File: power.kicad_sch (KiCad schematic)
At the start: 8 parts, among them J3 Screw_Terminal_01x02, J4 Screw_Terminal_01x02, U8 AZ1117CH-5.0TRG1, U9 LD29150DT33R

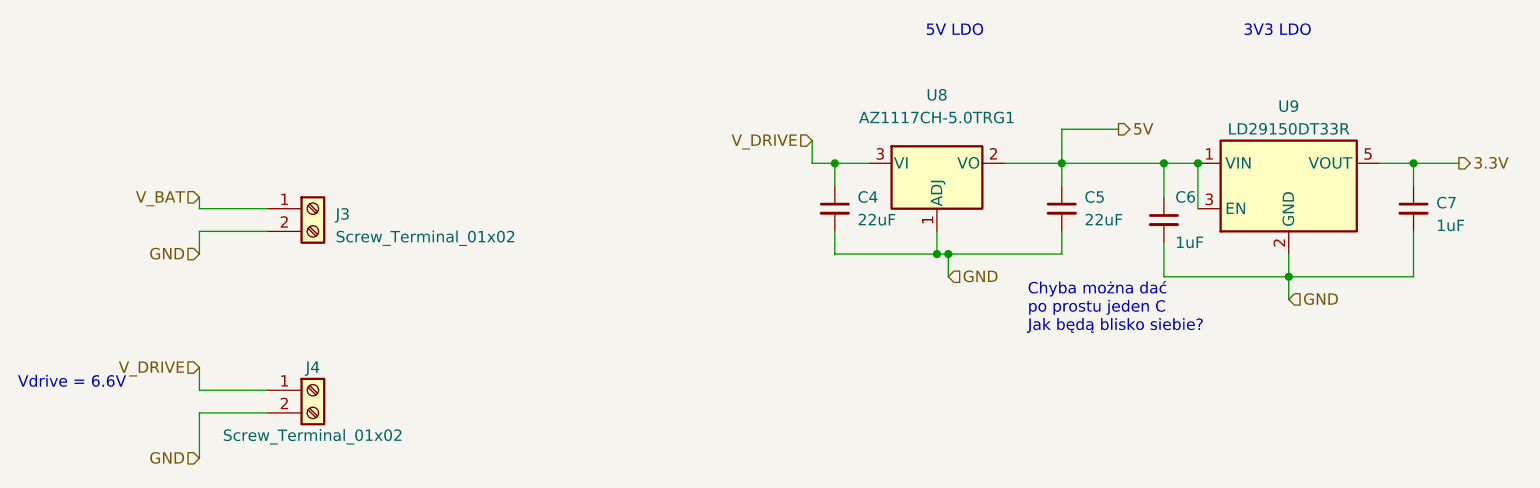
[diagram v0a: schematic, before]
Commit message: Bord v1.2, added flash memory, changed pinout od servomotor connectors and removed potentiometer signal from servomotors plus one ADC
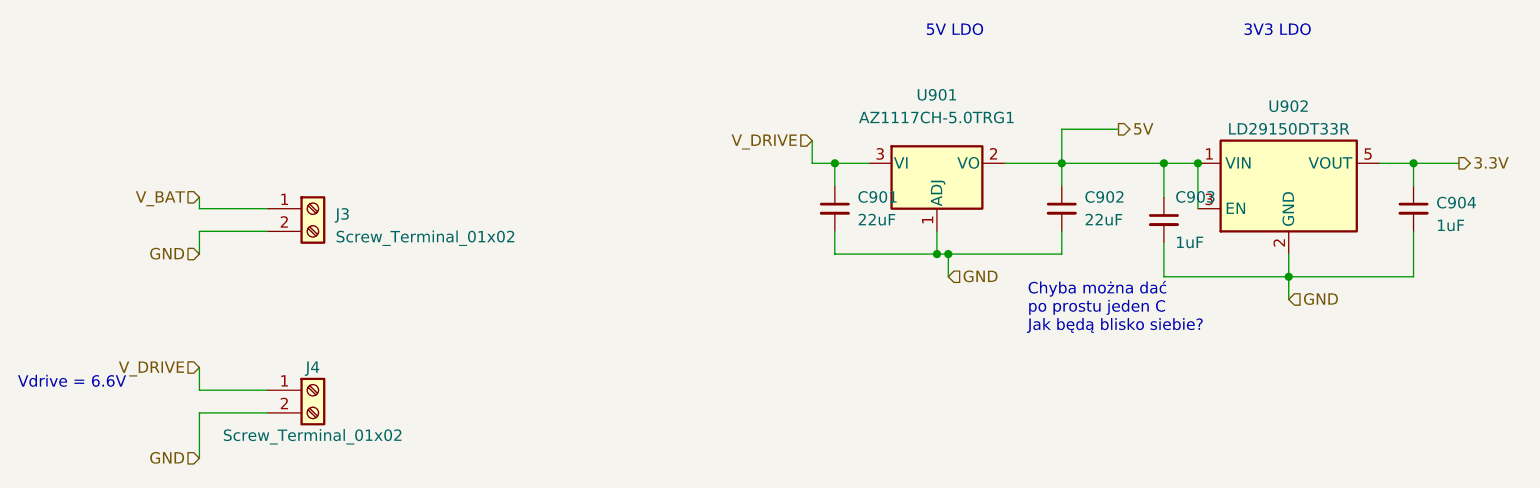
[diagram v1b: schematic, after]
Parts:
- renumbered C4 to C901, C5 to C902, C6 to C903, C7 to C904, U8 to U901, U9 to U902
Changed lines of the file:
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@@
   (symbol (lib_id "Device:C_Small") (at 156.21 63.5 0) (unit 1)
     (in_bom yes) (on_board yes) (dnp no)
-    (property "Reference" "C6" (at 157.48 60.96 0)
+    (property "Reference" "C903" (at 157.48 60.96 0)
       (effects (font (size 1.27 1.27)) (justify left))
     )
@@
       (project "Hexapod_Hardware"
         (path "/04005f68-61ba-4735-aba3-9cac296c0cce/2b79a7de-52ea-4f31-b6a5-c4c613c567f9"
+          (reference "C903") (unit 1)
+        )
+      )
+      (project "test_ADC_and_CurrentSensors"
+        (path "/11442fd4-c5b6-4318-b48c-3e08ddc782a8/1783009b-3fd4-4eb2-9eed-12da5fa53b67"
           (reference "C6") (unit 1)
         )
       )
-      (project "test_ADC_and_CurrentSensors"
-        (path "/11442fd4-c5b6-4318-b48c-3e08ddc782a8/1783009b-3fd4-4eb2-9eed-12da5fa53b67"
+      (project "combat_2.0"
+        (path "/518cdd36-e3d2-496e-a534-90a14dea15b3"
           (reference "C6") (unit 1)
         )
       )
-      (project "combat_2.0"
-        (path "/518cdd36-e3d2-496e-a534-90a14dea15b3"
-          (reference "C6") (unit 1)
-        )
-      )
     )
   )
   (symbol (lib_id "Device:C_Small") (at 144.78 62.23 0) (unit 1)
     (in_bom yes) (on_board yes) (dnp no) (fields_autoplaced)
-    (property "Reference" "C5" (at 147.32 60.9662 0)
+    (property "Reference" "C902" (at 147.32 60.9662 0)
       (effects (font (size 1.27 1.27)) (justify left))
     )
@@
       (project "Hexapod_Hardware"
         (path "/04005f68-61ba-4735-aba3-9cac296c0cce/2b79a7de-52ea-4f31-b6a5-c4c613c567f9"
+          (reference "C902") (unit 1)
+        )
+      )
+      (project "test_ADC_and_CurrentSensors"
+        (path "/11442fd4-c5b6-4318-b48c-3e08ddc782a8/1783009b-3fd4-4eb2-9eed-12da5fa53b67"
           (reference "C5") (unit 1)
         )
       )
-      (project "test_ADC_and_CurrentSensors"
-        (path "/11442fd4-c5b6-4318-b48c-3e08ddc782a8/1783009b-3fd4-4eb2-9eed-12da5fa53b67"
-          (reference "C5") (unit 1)
-        )
-      )
       (project "combat_2.0"
         (path "/518cdd36-e3d2-496e-a534-90a14dea15b3"
@@
   (symbol (lib_id "Device:C_Small") (at 119.38 62.23 0) (unit 1)
     (in_bom yes) (on_board yes) (dnp no) (fields_autoplaced)
-    (property "Reference" "C4" (at 121.92 60.9662 0)
+    (property "Reference" "C901" (at 121.92 60.9662 0)
       (effects (font (size 1.27 1.27)) (justify left))
     )
@@
       (project "Hexapod_Hardware"
         (path "/04005f68-61ba-4735-aba3-9cac296c0cce/2b79a7de-52ea-4f31-b6a5-c4c613c567f9"
-          (reference "C4") (unit 1)
+          (reference "C901") (unit 1)
         )
       )
@@
         )
         (path "/04005f68-61ba-4735-aba3-9cac296c0cce/2b79a7de-52ea-4f31-b6a5-c4c613c567f9"
-          (reference "J18") (unit 1)
+          (reference "J901") (unit 1)
         )
       )
@@
   (symbol (lib_id "Regulator_Linear:MIC5366-3.3YC5") (at 170.18 59.69 0) (unit 1)
     (in_bom yes) (on_board yes) (dnp no) (fields_autoplaced)
-    (property "Reference" "U9" (at 170.18 50.8 0)
+    (property "Reference" "U902" (at 170.18 50.8 0)
       (effects (font (size 1.27 1.27)))
     )
@@
       (project "Hexapod_Hardware"
         (path "/04005f68-61ba-4735-aba3-9cac296c0cce/2b79a7de-52ea-4f31-b6a5-c4c613c567f9"
-          (reference "U9") (unit 1)
+          (reference "U902") (unit 1)
         )
       )
@@
   (symbol (lib_id "Device:C_Small") (at 184.15 62.23 0) (unit 1)
     (in_bom yes) (on_board yes) (dnp no) (fields_autoplaced)
-    (property "Reference" "C7" (at 186.69 61.6013 0)
+    (property "Reference" "C904" (at 186.69 61.6013 0)
       (effects (font (size 1.27 1.27)) (justify left))
     )
@@
       (project "Hexapod_Hardware"
         (path "/04005f68-61ba-4735-aba3-9cac296c0cce/2b79a7de-52ea-4f31-b6a5-c4c613c567f9"
-          (reference "C7") (unit 1)
+          (reference "C904") (unit 1)
         )
       )
@@
         )
         (path "/04005f68-61ba-4735-aba3-9cac296c0cce/2b79a7de-52ea-4f31-b6a5-c4c613c567f9"
-          (reference "J19") (unit 1)
+          (reference "J902") (unit 1)
         )
       )
@@
   (symbol (lib_id "Regulator_Linear:AZ1117H-ADJ") (at 130.81 57.15 0) (unit 1)
     (in_bom yes) (on_board yes) (dnp no) (fields_autoplaced)
-    (property "Reference" "U8" (at 130.81 49.53 0)
+    (property "Reference" "U901" (at 130.81 49.53 0)
       (effects (font (size 1.27 1.27)))
     )
@@
       (project "Hexapod_Hardware"
         (path "/04005f68-61ba-4735-aba3-9cac296c0cce/2b79a7de-52ea-4f31-b6a5-c4c613c567f9"
-          (reference "U8") (unit 1)
-        )
-      )
+          (reference "U901") (unit 1)
+        )
+      )
